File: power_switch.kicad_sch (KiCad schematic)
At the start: 14 parts, among them J3 Power Input, J4 Power Output, U1 BTS7004-1EPP

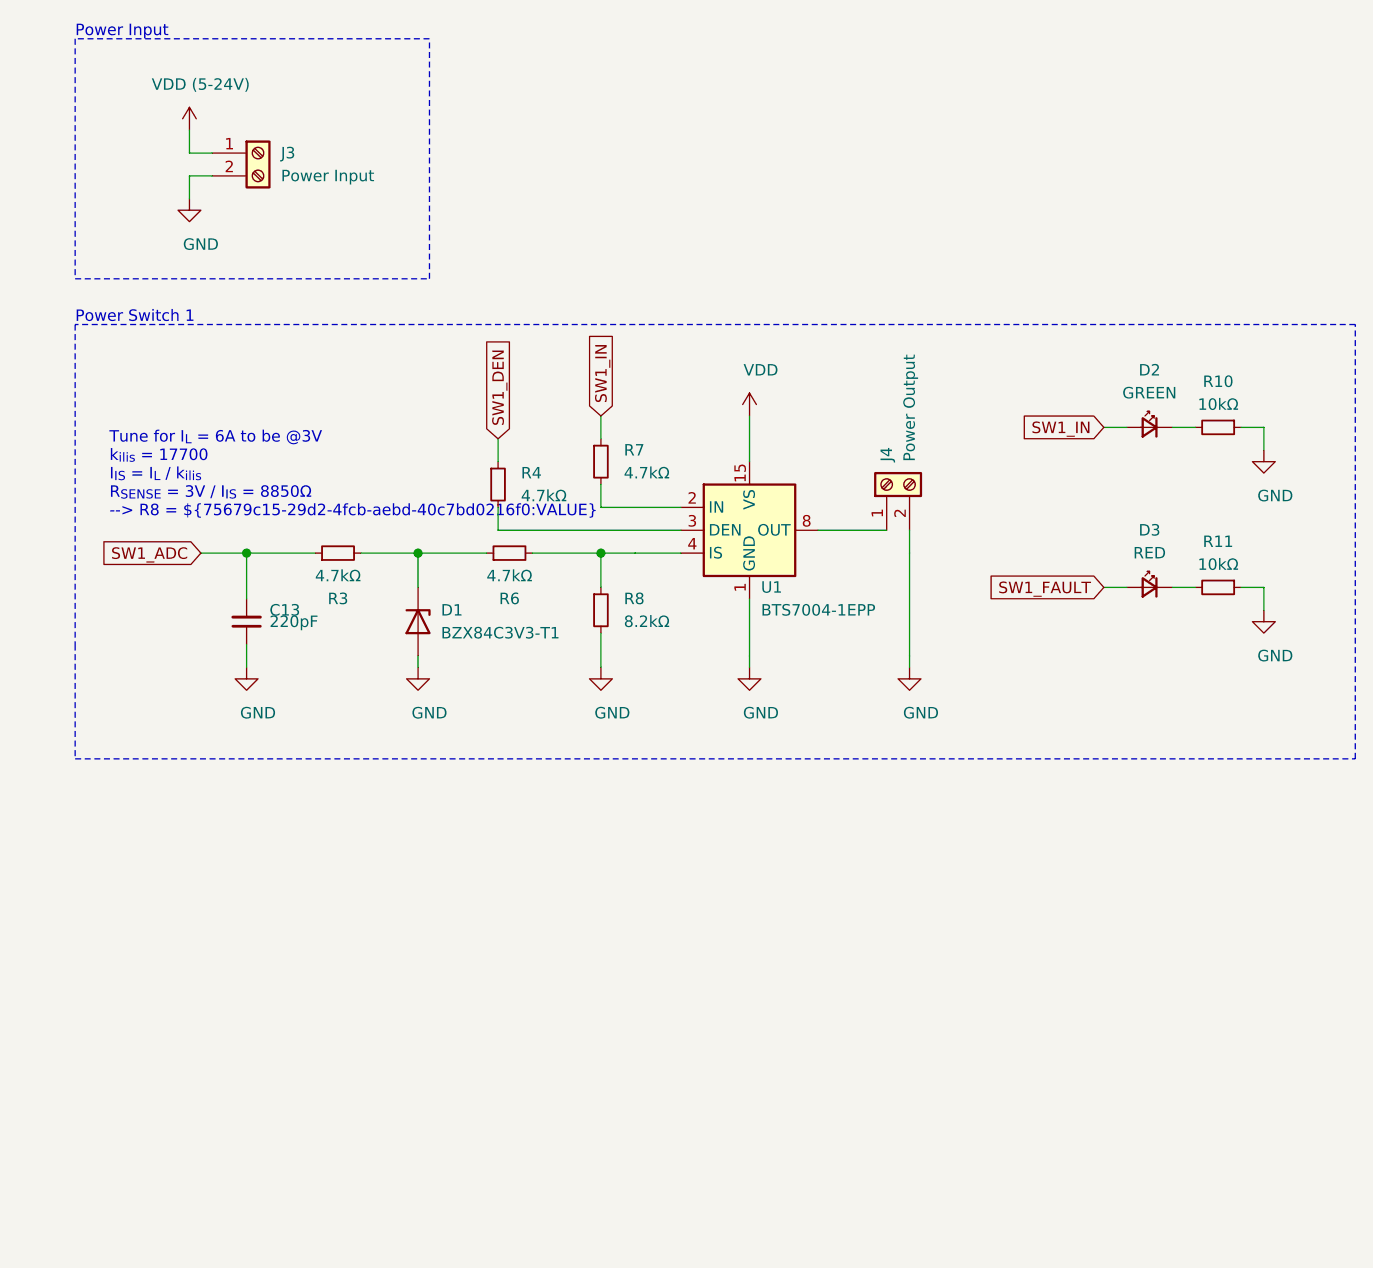
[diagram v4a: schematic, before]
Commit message: add voltage measurement
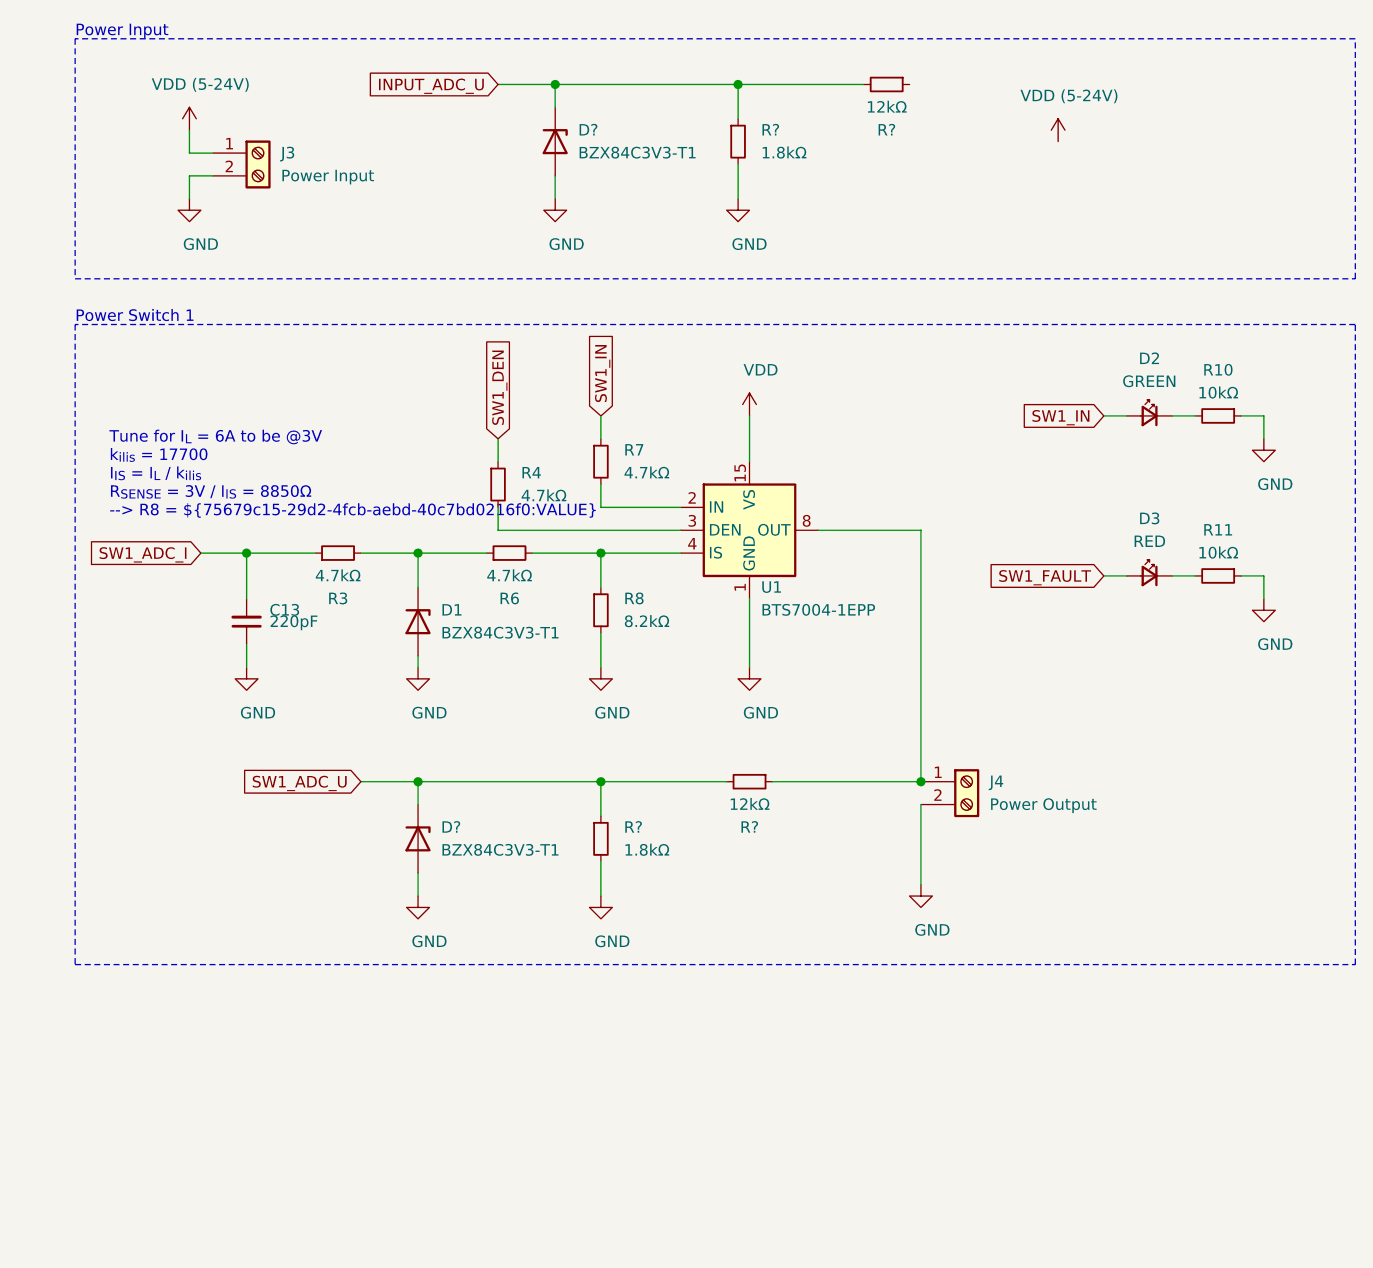
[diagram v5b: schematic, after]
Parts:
- added D? (x2): BZX84C3V3-T1, Diode_SMD:D_SOT-23_ANK, symbol Diode:DZ2S033X0L
- added R? (x2): 12kΩ, symbol Device:R_Small
- added R? (x2): 1.8kΩ, symbol Device:R_Small
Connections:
- net GND: now also D?.2 (A), D?.2 (A), R?.2, R?.2
- net at J4.1 (Pin_1), U1.10 (OUT), U1.12 (OUT)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: now also R?.1
- net SW1_ADC renamed SW1_ADC_I
- new net INPUT_ADC_U: D?.1 (K), R?.1, R?.2
- new net SW1_ADC_U: D?.1 (K), R?.1, R?.2
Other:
- moved on the sheet: D2, D3, J4, R10, R11

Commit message: introduce hierarchical sheets for power switches
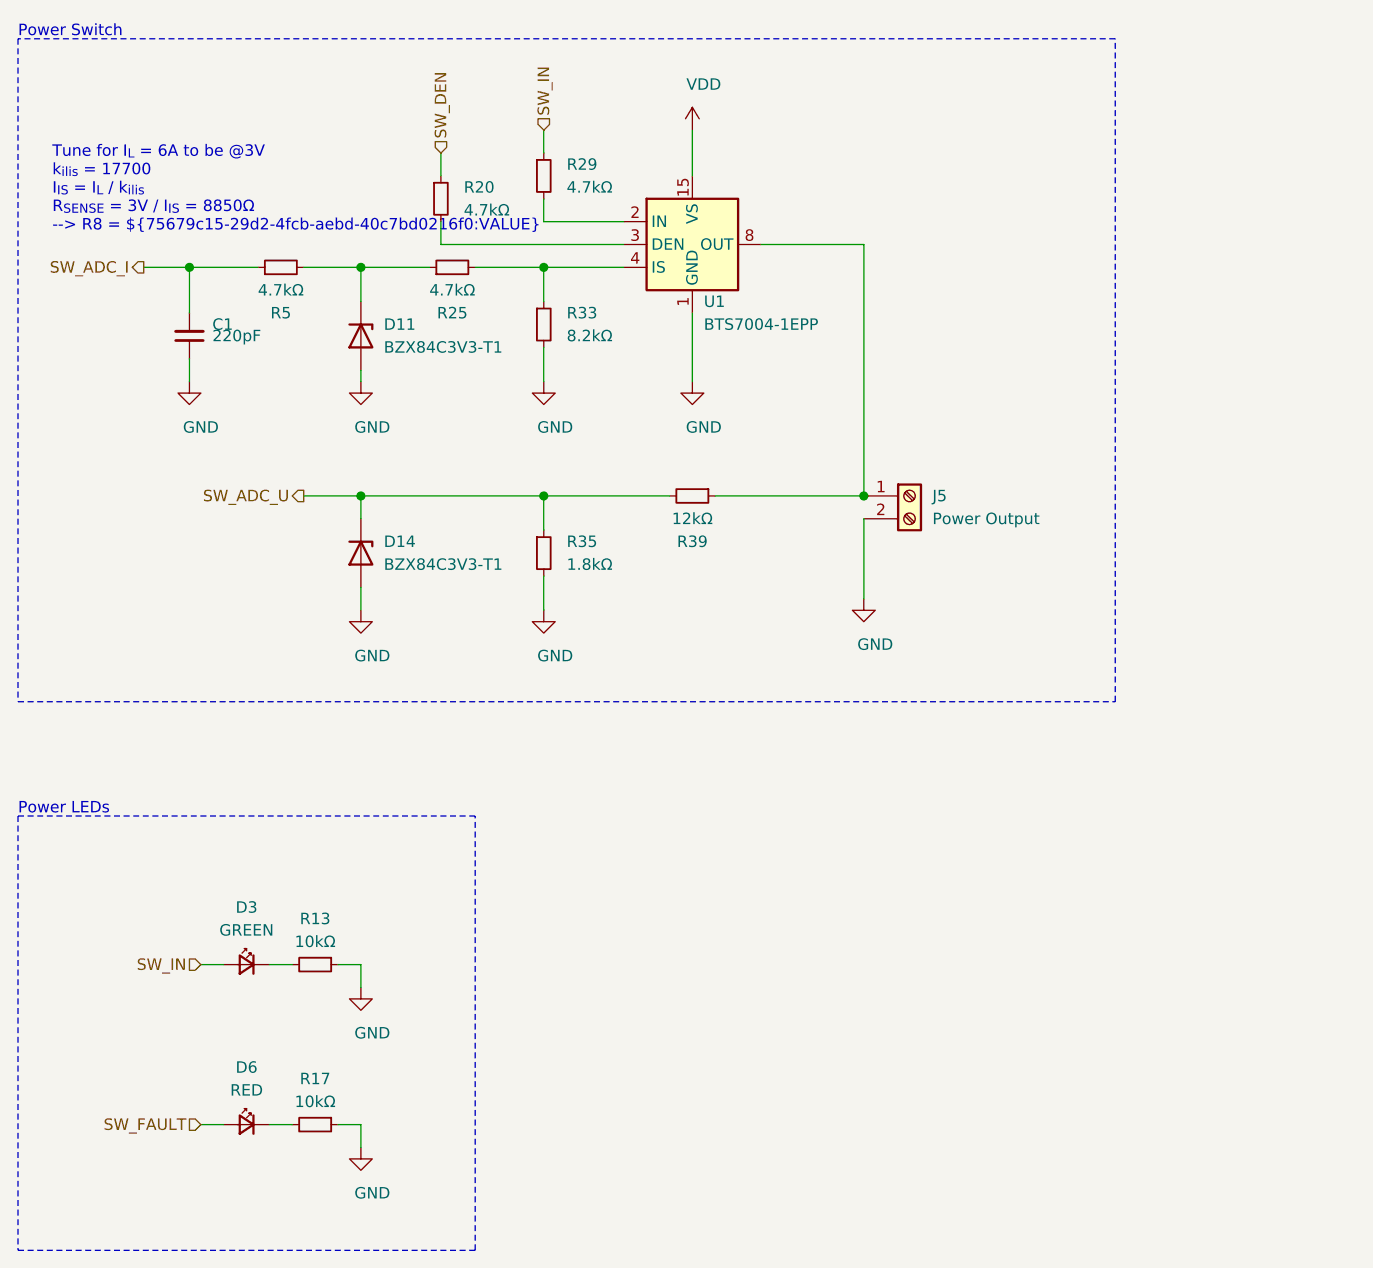
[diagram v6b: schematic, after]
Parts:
- removed D2: GREEN, LED_SMD:LED_0402_1005Metric, symbol Device:LED_Small
- removed D?: BZX84C3V3-T1, Diode_SMD:D_SOT-23_ANK, symbol Diode:DZ2S033X0L
- removed J3: Power Input, TerminalBlock_RND:TerminalBlock_RND_205-00287_1x02_P5.08mm_Horizontal, symbol Connector:Screw_Terminal_01x02
- removed R10, R11: 10kΩ, Resistor_SMD:R_0402_1005Metric, symbol Device:R_Small
- removed R?: 12kΩ, symbol Device:R_Small
- removed R?: 1.8kΩ, symbol Device:R_Small
- added D6: RED, LED_SMD:LED_0603_1608Metric, symbol Device:LED_Small
- added R13, R17: 10kΩ, Resistor_SMD:R_0603_1608Metric, symbol Device:R_Small
- C1: renamed from C13; footprint Capacitor_SMD:C_0402_1005Metric -> Capacitor_SMD:C_0603_1608Metric
- D3: value RED -> GREEN; footprint LED_SMD:LED_0402_1005Metric -> LED_SMD:LED_0603_1608Metric
- R20: renamed from R4; footprint Resistor_SMD:R_0402_1005Metric -> Resistor_SMD:R_0603_1608Metric
- R25: renamed from R6; footprint Resistor_SMD:R_0402_1005Metric -> Resistor_SMD:R_0603_1608Metric
- R29: renamed from R7; footprint Resistor_SMD:R_0402_1005Metric -> Resistor_SMD:R_0603_1608Metric
- R33: renamed from R8; footprint Resistor_SMD:R_0402_1005Metric -> Resistor_SMD:R_0603_1608Metric
- R35, R39: renamed from R?; footprint (none) -> Resistor_SMD:R_0603_1608Metric
- R5: renamed from R3; footprint Resistor_SMD:R_0402_1005Metric -> Resistor_SMD:R_0603_1608Metric
- gave numbers to parts that had none: 1
- renumbered D1 to D11, J4 to J5
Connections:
- net SW1_IN is gone; now on net SW_IN: R29.1
- net GND: now also R13.1, R17.1
- net at D3.1 (K): now also R13.2
- net SW1_ADC_I renamed SW_ADC_I
- net SW1_ADC_U renamed SW_ADC_U
- net SW1_DEN renamed SW_DEN
- net SW1_FAULT renamed SW_IN
- new net: D6.1 (K), R17.2
- new net SW_FAULT: D6.2 (A)
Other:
- note added: "Power LEDs"
- note added: "Power Switch"
- note removed: "Power Input"
- note removed: "Power Switch 1"
- moved on the sheet: C1, D11, D14, J5, R20, R25, R29, R33, R35, R39, R5, U1

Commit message: initial component placement
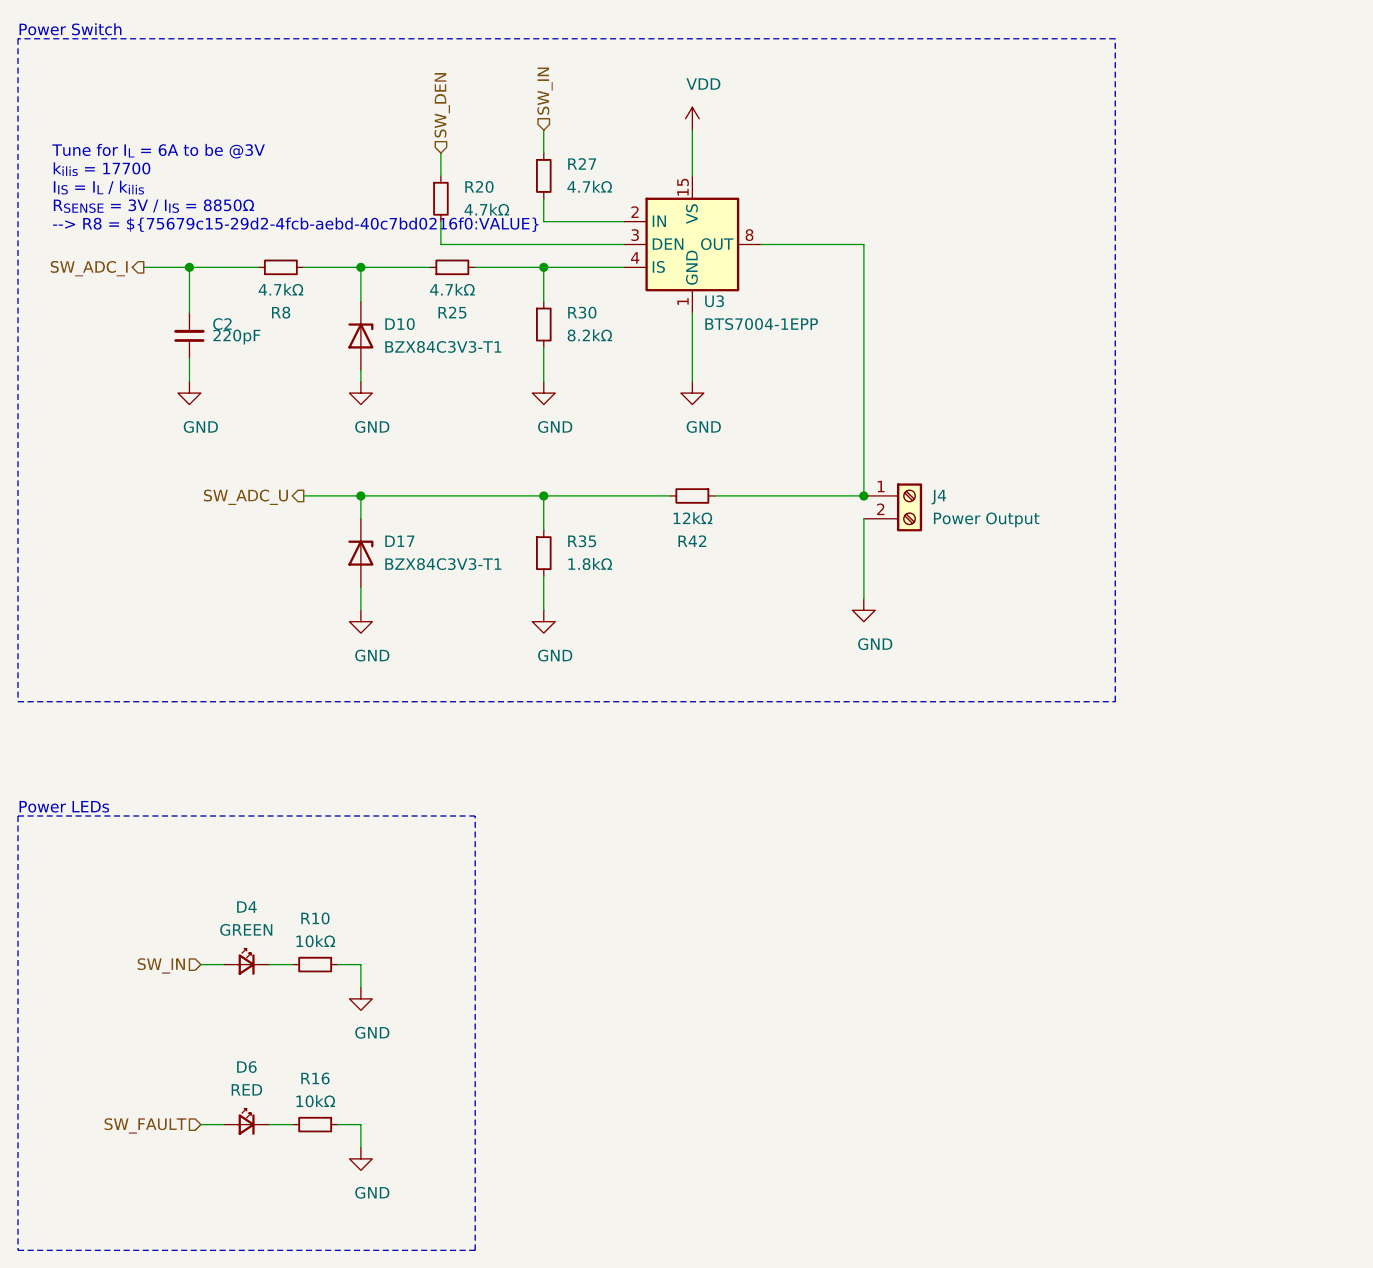
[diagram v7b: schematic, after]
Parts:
- renumbered C1 to C2, D11 to D10, D14 to D17, D3 to D4, J5 to J4, R13 to R10, R17 to R16, R29 to R27, R33 to R30, R39 to R42, R5 to R8, U1 to U3
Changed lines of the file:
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@@
   (page 0 7)
   (paper "A4")
+  (title_block
+    (comment 4 "Author: Stefan Agner")
+  )
   (junction (at 38.1 44.45) (diameter 1.016) (color 0 0 0 0))
   (junction (at 57.15 44.45) (diameter 1.016) (color 0 0 0 0))
@@
   (symbol (lib_id "power:GND") (at 57.15 57.15 0)
     (in_bom yes) (on_board yes)
-    (property "Reference" "#PWR021" (id 0) (at 57.15 63.5 0)
+    (property "Reference" "#PWR019" (id 0) (at 57.15 63.5 0)
       (effects (font (size 1.27 1.27)) hide)
     )
@@
   (symbol (lib_id "power:GND") (at 57.15 124.46 0)
     (in_bom yes) (on_board yes)
-    (property "Reference" "#PWR028" (id 0) (at 57.15 130.81 0)
+    (property "Reference" "#PWR026" (id 0) (at 57.15 130.81 0)
       (effects (font (size 1.27 1.27)) hide)
     )
@@
   (symbol (lib_id "power:GND") (at 57.15 142.24 0)
     (in_bom yes) (on_board yes)
-    (property "Reference" "#PWR032" (id 0) (at 57.15 148.59 0)
+    (property "Reference" "#PWR033" (id 0) (at 57.15 148.59 0)
       (effects (font (size 1.27 1.27)) hide)
     )
@@
   (symbol (lib_id "power:GND") (at 77.47 57.15 0)
     (in_bom yes) (on_board yes)
-    (property "Reference" "#PWR038" (id 0) (at 77.47 63.5 0)
+    (property "Reference" "#PWR037" (id 0) (at 77.47 63.5 0)
       (effects (font (size 1.27 1.27)) hide)
     )
@@
   (symbol (lib_id "power:GND") (at 77.47 82.55 0)
     (in_bom yes) (on_board yes)
-    (property "Reference" "#PWR041" (id 0) (at 77.47 88.9 0)
+    (property "Reference" "#PWR040" (id 0) (at 77.47 88.9 0)
       (effects (font (size 1.27 1.27)) hide)
     )
@@
   (symbol (lib_id "power:GND") (at 93.98 57.15 0)
     (in_bom yes) (on_board yes)
-    (property "Reference" "#PWR049" (id 0) (at 93.98 63.5 0)
+    (property "Reference" "#PWR051" (id 0) (at 93.98 63.5 0)
       (effects (font (size 1.27 1.27)) hide)
     )
@@
   (symbol (lib_id "Device:R_Small") (at 48.26 44.45 90)
     (in_bom yes) (on_board yes)
-    (property "Reference" "R5" (id 0) (at 48.26 49.53 90))
+    (property "Reference" "R8" (id 0) (at 48.26 49.53 90))
     (property "Value" "4.7kΩ" (id 1) (at 48.26 46.99 90))
     (property "Footprint" "Resistor_SMD:R_0603_1608Metric" (id 2) (at 48.26 46.228 90)
@@
   (symbol (lib_id "Device:R_Small") (at 52.07 121.92 270)
     (in_bom yes) (on_board yes)
-    (property "Reference" "R13" (id 0) (at 52.07 116.84 90))
+    (property "Reference" "R10" (id 0) (at 52.07 116.84 90))
     (property "Value" "10kΩ" (id 1) (at 52.07 119.38 90))
     (property "Footprint" "Resistor_SMD:R_0603_1608Metric" (id 2) (at 52.07 120.142 90)
@@
   (symbol (lib_id "Device:R_Small") (at 52.07 139.7 270)
     (in_bom yes) (on_board yes)
-    (property "Reference" "R17" (id 0) (at 52.07 134.62 90))
+    (property "Reference" "R16" (id 0) (at 52.07 134.62 90))
     (property "Value" "10kΩ" (id 1) (at 52.07 137.16 90))
     (property "Footprint" "Resistor_SMD:R_0603_1608Metric" (id 2) (at 52.07 137.922 90)
@@
   (symbol (lib_id "Device:R_Small") (at 77.47 34.29 0)
     (in_bom yes) (on_board yes)
-    (property "Reference" "R29" (id 0) (at 80.01 33.02 0)
+    (property "Reference" "R27" (id 0) (at 80.01 33.02 0)
       (effects (font (size 1.27 1.27)) (justify left))
     )
@@
   (symbol (lib_id "Device:R_Small") (at 77.47 50.8 0)
     (in_bom yes) (on_board yes)
-    (property "Reference" "R33" (id 0) (at 80.01 49.53 0)
+    (property "Reference" "R30" (id 0) (at 80.01 49.53 0)
       (effects (font (size 1.27 1.27)) (justify left))
     )
@@
   (symbol (lib_id "Device:R_Small") (at 93.98 69.85 270)
     (in_bom yes) (on_board yes)
-    (property "Reference" "R39" (id 0) (at 93.98 74.93 90))
+    (property "Reference" "R42" (id 0) (at 93.98 74.93 90))
     (property "Value" "12kΩ" (id 1) (at 93.98 72.39 90))
     (property "Footprint" "Resistor_SMD:R_0603_1608Metric" (id 2) (at 93.98 69.85 0)
@@
   (symbol (lib_id "Device:LED_Small") (at 44.45 121.92 0) (mirror y)
     (in_bom yes) (on_board yes)
-    (property "Reference" "D3" (id 0) (at 44.45 115.57 0))
+    (property "Reference" "D4" (id 0) (at 44.45 115.57 0))
     (property "Value" "GREEN" (id 1) (at 44.45 118.11 0))
     (property "Footprint" "LED_SMD:LED_0603_1608Metric" (id 2) (at 44.45 121.92 90)
@@
   (symbol (lib_id "Device:C_Small") (at 38.1 52.07 180)
     (in_bom yes) (on_board yes)
-    (property "Reference" "C1" (id 0) (at 40.64 50.8 0)
+    (property "Reference" "C2" (id 0) (at 40.64 50.8 0)
       (effects (font (size 1.27 1.27)) (justify right))
     )
@@
   (symbol (lib_id "Diode:DZ2S033X0L") (at 57.15 52.07 270)
     (in_bom yes) (on_board yes)
-    (property "Reference" "D11" (id 0) (at 59.69 50.8 90)
+    (property "Reference" "D10" (id 0) (at 59.69 50.8 90)
       (effects (font (size 1.27 1.27)) (justify left))
     )
@@
   (symbol (lib_id "Diode:DZ2S033X0L") (at 57.15 76.2 270)
     (in_bom yes) (on_board yes)
-    (property "Reference" "D14" (id 0) (at 59.69 74.93 90)
+    (property "Reference" "D17" (id 0) (at 59.69 74.93 90)
       (effects (font (size 1.27 1.27)) (justify left))
     )
@@
   (symbol (lib_id "Connector:Screw_Terminal_01x02") (at 118.11 69.85 0)
     (in_bom yes) (on_board yes)
-    (property "Reference" "J5" (id 0) (at 120.65 69.85 0)
+    (property "Reference" "J4" (id 0) (at 120.65 69.85 0)
       (effects (font (size 1.27 1.27)) (justify left))
     )
@@
   (symbol (lib_id "Power_Management:BTS7004-1EPP") (at 93.98 41.91 0)
     (in_bom yes) (on_board yes)
-    (property "Reference" "U1" (id 0) (at 95.25 48.26 0)
-      (effects (font (size 1.27 1.27)) (justify left))
-    )
+    (property "Reference" "U3" (id 0) (at 95.25 48.26 0)
+      (effects (font (size 1.27 1.27)) (justify left))
+    )
